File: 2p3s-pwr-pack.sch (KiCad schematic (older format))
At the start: 16 parts, among them P1 PAD, P10 PAD, P11 PAD, P12 PAD, P2 PAD, P3 PAD, P4 PAD, P5 PAD, P6 PAD, P7 PAD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

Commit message: 2019-03018 ready for ordering.
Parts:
- added MOD2: Module_AliExpress_BMS_3s_Balancing-3S0404LI502, Modulez:Module_BMS_Balancing_3s_AliExpress_BMS-3S0404LI502, symbol __Power:Module_AliExpress_BMS_3s_Balancing-3S0404LI502
- added P13: Conn_Basic_2_pin, Footprints:TERM_BLK_2_SIDE_2.54MM, symbol __Interfaces:Conn_Basic_2_pin
- added P14, P15: PAD, Footprints:HOLE_4mmx2.2mm, symbol __SimpleParts:PAD
- P1, P10, P11, P12, P2, P3, P4, P5, P6, P7, P8, P9: footprint NPTH_3mm -> NPTH_5mm
- renumbered BATT3 to BATT1, BATT1 to BATT3
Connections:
- net labels added: B+, P+, P+_SW, V_IN
- wire segments 22 -> 55
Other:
- note added: "2p3s"
- note added: "3s Balancing"
- note added: "BMS"
- note added: "Barrel Jack"
- note added: "Battery Holders"
- note added: "DC/DC Buck\nCC/CV Module"
- note added: "External Power Input"
- note added: "NOTE TO MAX"
- note added: "PCB Connection Points"
- note added: "Switches in JIRA issue are SPST MOMENTARY switches"
- note added: "Terminal Block"
- note added: "discuss switch operation, what gets switched. charging, operation? both? (DPDT)"
- note removed: "ADD SCREW HEADERS FOR POWER INPUT"
- note removed: "HOLES FOR THE BUTTON INPUTS"
- moved on the sheet: BATT1, BATT2, BATT3, MOD1, P1, P10, P11, P12, P2, P3, P4, P5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

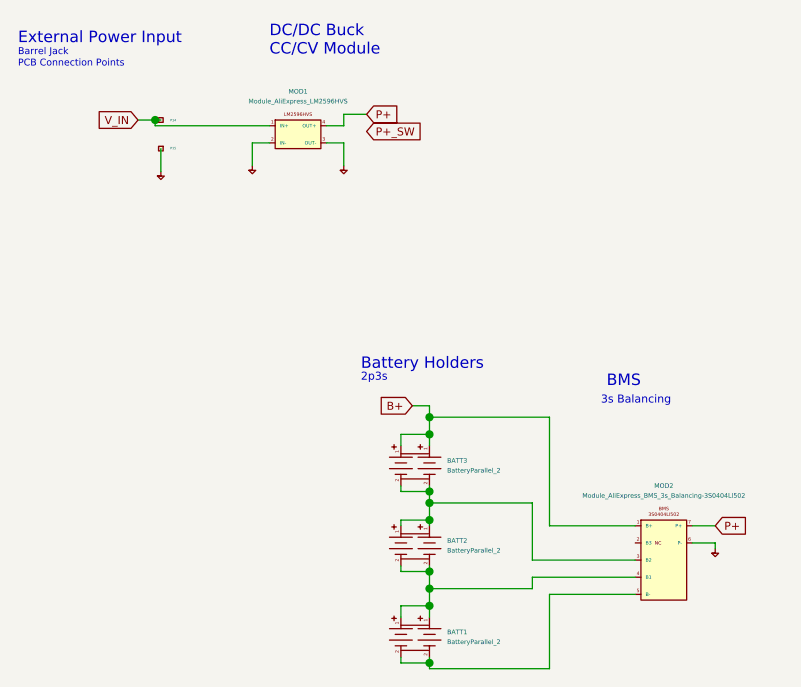
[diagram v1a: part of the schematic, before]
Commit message: Schematic, PCB changes
Move holder 3 1mm West, holder 2 2mm west, holder 1 3mm west.

SMA schottky diode on output of CC/CV.
Fix B1/B3 mixup on BMS
CC/CV input (-) no longer tied to GND (defeats CC mode)
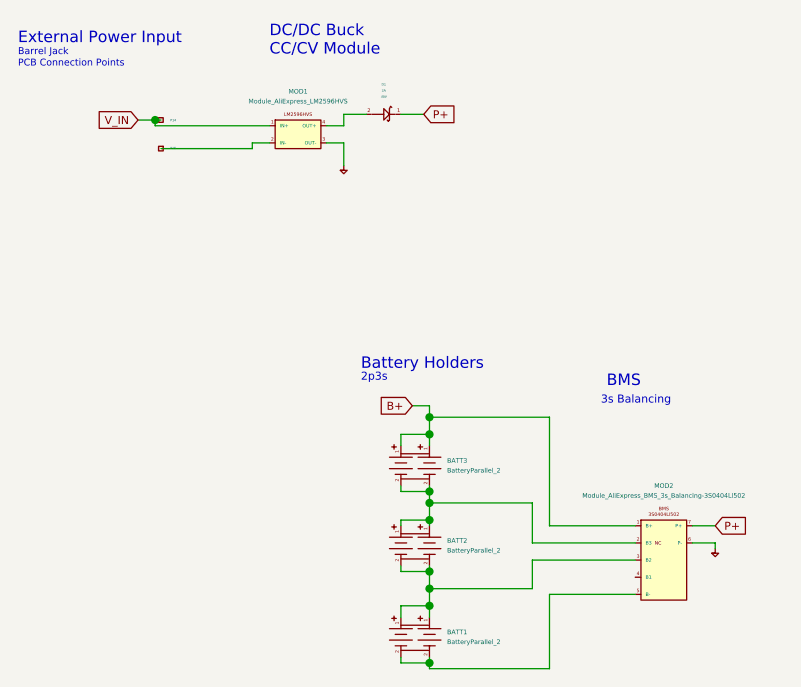
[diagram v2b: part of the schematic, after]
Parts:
- added D1: 2A, Footprints:SMA, symbol __SimpleParts:Diode_Schottky
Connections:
- net GND1: no longer MOD1.2 (IN-), P15.1
- net P+: now also D1.1; no longer MOD1.4 (OUT+)
- net at BATT2.1, BATT3.2: now also MOD2.2 (B3); no longer MOD2.3 (B2)
- net at BATT1.1, BATT2.2: now also MOD2.3 (B2); no longer MOD2.4 (B1)
- new net: MOD1.2 (IN-), P15.1
- new net: D1.2, MOD1.4 (OUT+)
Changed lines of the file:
@@
 EESchema Schematic File Version 4
+LIBS:2p3s-pwr-pack-cache
 EELAYER 26 0
 EELAYER END
@@
 Wire Wire Line
 	1625 3250 1700 3250
-$Comp
-L __SimpleParts:GND #PWR0101
-U 1 1 5CB01D8A
-P 1725 3475
-F 0 "#PWR0101" H 1700 3460 5   0001 C CNN
-F 1 "GND" H 1695 3470 5   0001 C CNN
-F 2 "" H 1725 3475 50  0000 C CNN
-F 3 "" H 1725 3475 50  0000 C CNN
-	1    1725 3475
-	1    0    0    -1
-$EndComp
-Wire Wire Line
-	1725 3475 1725 3375
 Wire Wire Line
 	2200 3275 1700 3275
@@
 Wire Wire Line
 	1700 3250 1725 3250
-$Comp
-L __SimpleParts:GND #PWR0105
-U 1 1 5CB04EA4
-P 2125 3450
-F 0 "#PWR0105" H 2100 3435 5   0001 C CNN
-F 1 "GND" H 2095 3445 5   0001 C CNN
-F 2 "" H 2125 3450 50  0000 C CNN
-F 3 "" H 2125 3450 50  0000 C CNN
-	1    2125 3450
-	1    0    0    -1
-$EndComp
-Wire Wire Line
-	2125 3450 2125 3350
 Wire Wire Line
 	2125 3350 2200 3350
@@
 Text Notes 2600 4400 0    35   ~ 0
 2p3s
-Wire Wire Line
-	3800 5175 3350 5175
 Text GLabel 4150 5025 2    35   Input ~ 0
 P+
@@
 Wire Wire Line
 	2900 4550 2900 4625
-Text GLabel 2625 3300 2    35   Input ~ 0
-P+_SW
-Text GLabel 2625 3225 2    35   Input ~ 0
+Text GLabel 2875 3225 2    35   Input ~ 0
 P+
 Wire Wire Line
@@
 Wire Wire Line
 	2900 5225 2900 5300
-Wire Wire Line
-	3350 5175 3350 4925
 Wire Wire Line
 	3350 4925 2900 4925
@@
 	2900 4925 2900 5000
 Wire Wire Line
-	3350 5250 3350 5300
-Wire Wire Line
 	3350 5300 2900 5300
 Connection ~ 2900 5300
 Wire Wire Line
 	2900 5300 2900 5375
-Wire Wire Line
-	3350 5250 3800 5250
 Wire Wire Line
 	3800 5325 3425 5325
@@
 Text Notes 2200 2975 0    50   ~ 0
 DC/DC Buck\nCC/CV Module
+$Comp
+L __SimpleParts:Diode_Schottky D1
+U 1 1 5CB5516F
+P 2700 3225
+F 0 "D1" V 2569 3225 10  0000 C CNN
+F 1 "2A " V 2596 3225 10  0000 C CNN
+F 2 "Footprints:SMA" H 2700 3125 60  0001 C CNN
+F 3 "" H 2700 3125 60  0001 C CNN
+F 4 "40V" V 2623 3225 10  0000 C CIN "Voltage"
+F 5 "Diodes Inc" H 2725 3275 10  0001 C CNN "Manufacturer1"
+F 6 "B240AE-13" H 2725 3200 10  0001 C CNN "Manufacturer1PartNumber"
+	1    2700 3225
+	0    1    1    0
+$EndComp
+Wire Wire Line
+	2875 3225 2775 3225
+Wire Wire Line
+	3800 5100 3350 5100
+Wire Wire Line
+	3350 5100 3350 4925
+Wire Wire Line
+	3350 5175 3800 5175
+Wire Wire Line
+	3350 5175 3350 5300
+Wire Wire Line
+	1725 3375 2125 3375
+Wire Wire Line
+	2125 3375 2125 3350
 $EndSCHEMATC
